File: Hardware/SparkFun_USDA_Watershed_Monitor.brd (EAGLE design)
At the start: 63.5 x 63.5 mm, 234 parts, among them J10 QWIIC_RIGHT_ANGLE, J3 QWIIC_RIGHT_ANGLE, J4 U.FL, J5 RJ45, J7 RJ45, J9 RJ45, Q1 20V/4.2A/52mΩ/1.4W, Q2 20V/0.2A/8MHz/1.2Ω/1Vth, Q3 20V/0.2A/8MHz/1.2Ω/1Vth, Q4 20V/0.2A/8MHz/1.2Ω/1Vth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

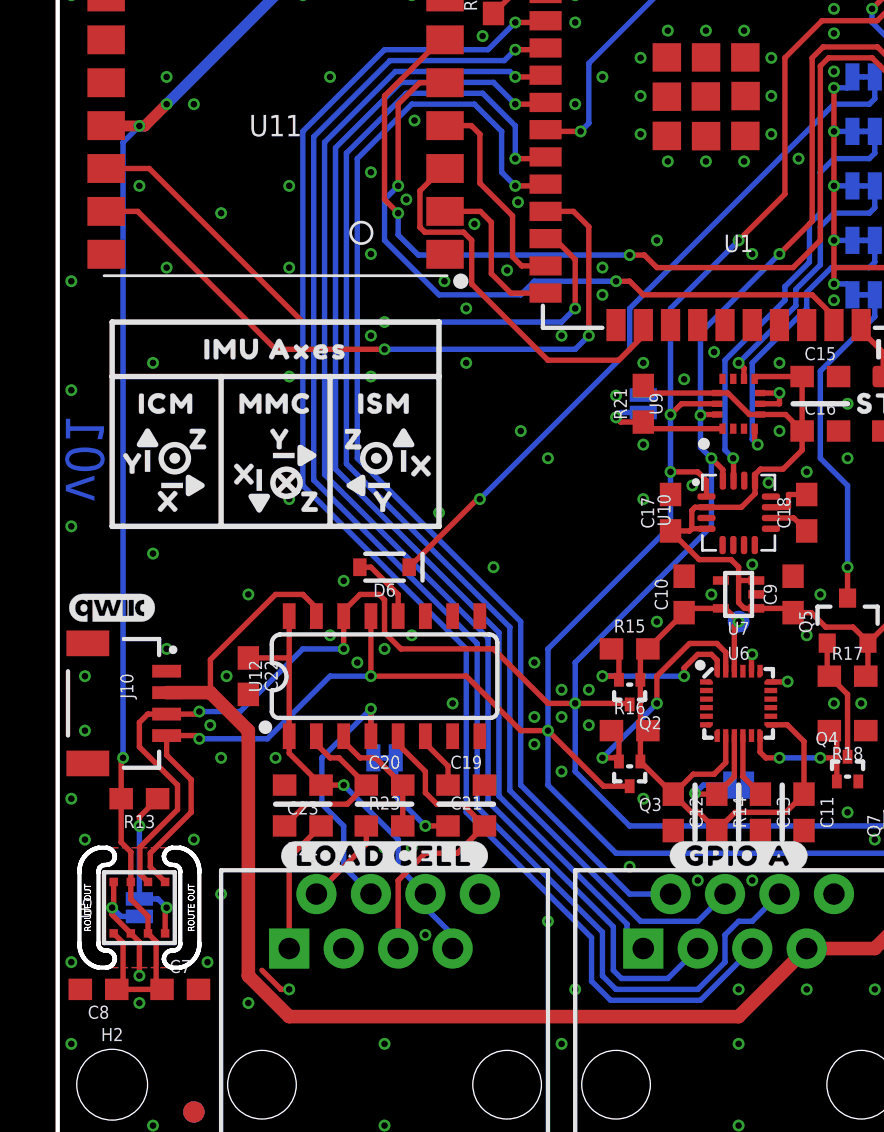
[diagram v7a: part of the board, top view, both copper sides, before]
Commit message: Add 3-pin JST connector for GPS
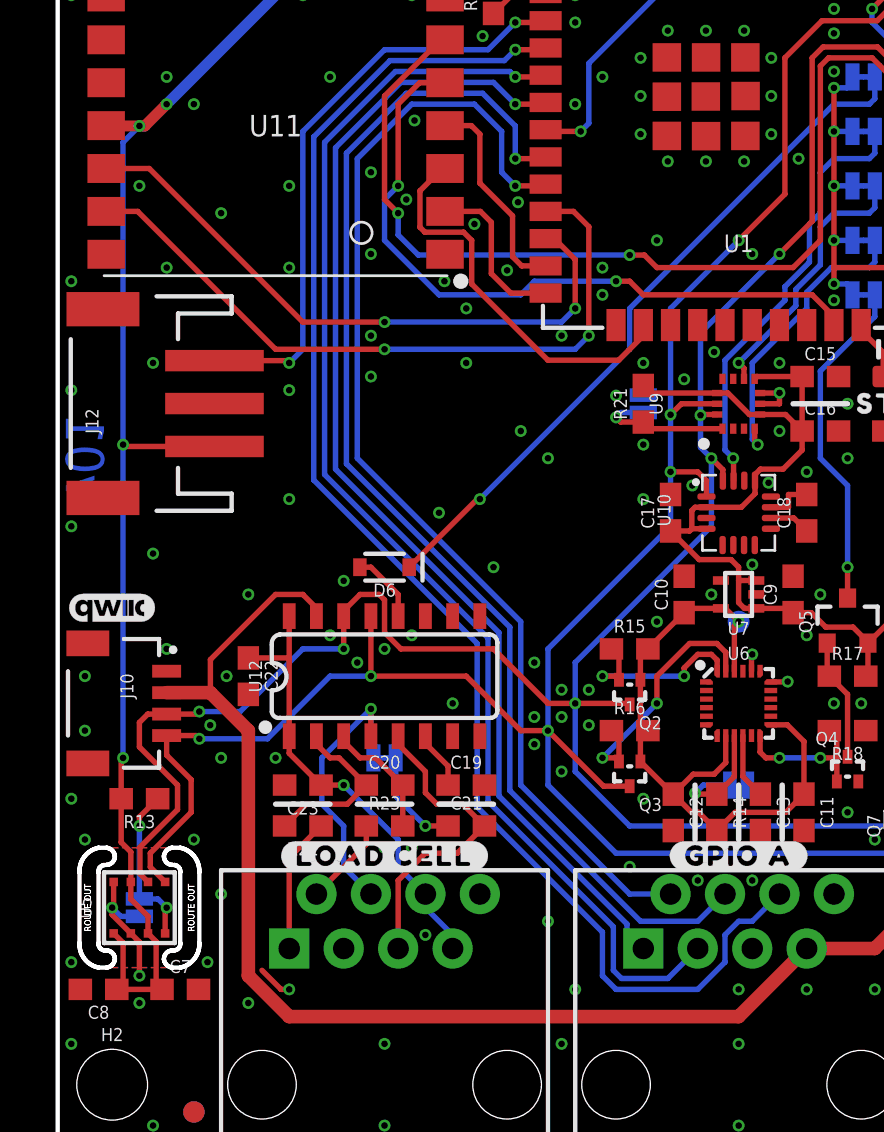
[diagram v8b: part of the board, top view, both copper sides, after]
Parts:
- removed U$101: (no value), output:IMU_AXES0
- removed U$88, U$91, U$94: (no value), output:X0
- removed U$89, U$92, U$95: (no value), output:Y0
- removed U$90, U$93, U$96: (no value), output:Z0
- removed U$97: (no value), output:ICM0
- removed U$98: (no value), output:ISM0
- removed U$99: (no value), output:MMC0
- added J12: 3-PIN SMD, SparkFun-Connectors:JST-3-SMD
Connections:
- net 3.3V: now also J12.3
- net ESP_I36: now also J12.1; no longer J7.5
- net GND: now also J12.2
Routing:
- net ESP_I36: track 67.5 -> 28.0 mm, vias 1 -> 2
- net 3.3V: track 247.8 -> 252.1 mm, vias 17 -> 18
